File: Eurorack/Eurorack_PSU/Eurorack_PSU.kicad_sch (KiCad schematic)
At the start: 18 parts, among them J1 AC, J2 AC, U1 LM7812_TO220, U2 LM7912_TO220

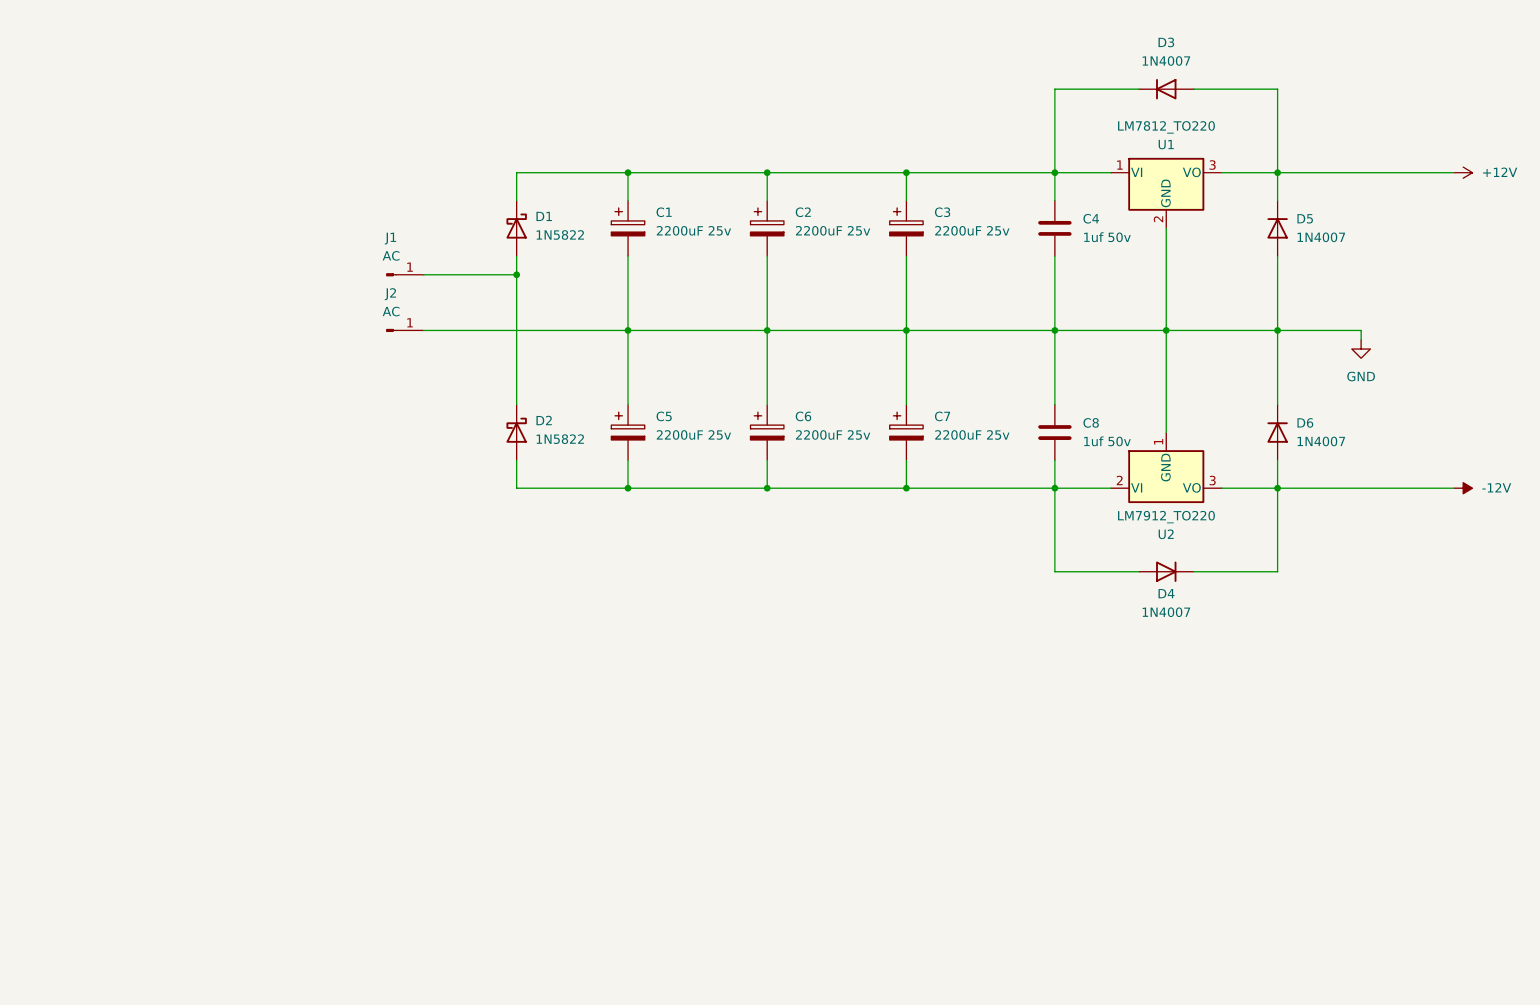
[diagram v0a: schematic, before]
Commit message: Update PSU and add more spice models
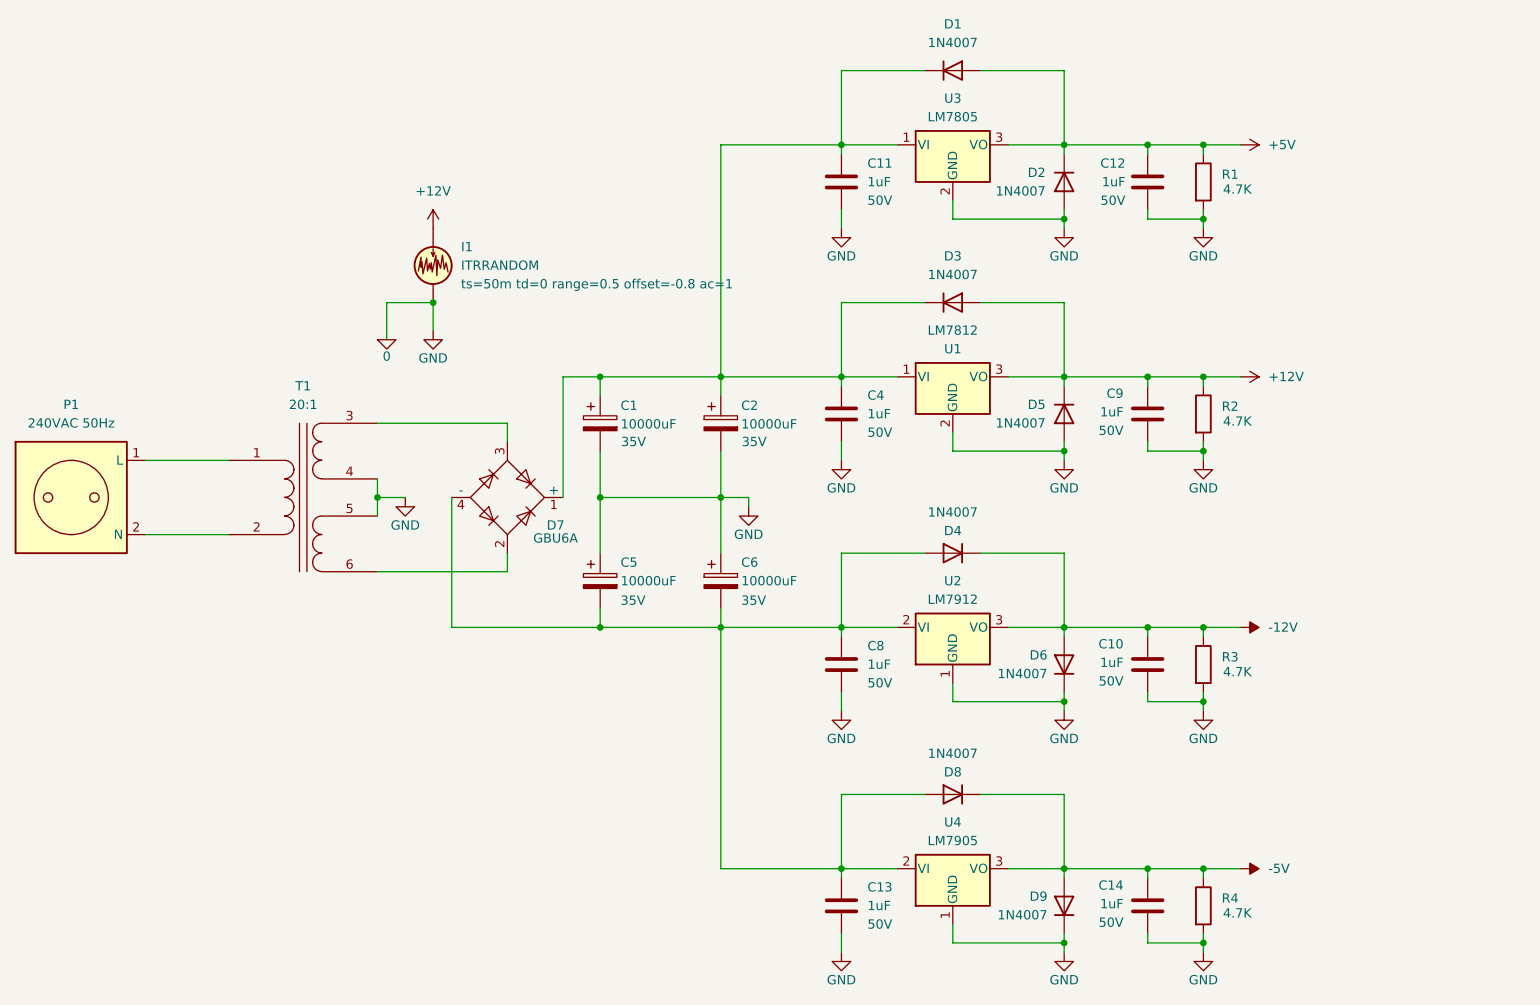
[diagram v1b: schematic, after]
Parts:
- removed C3, C7: 2200uF 25v, Capacitor_THT:CP_Radial_D16.0mm_P7.50mm, symbol Device:C_Polarized
- removed D1, D2: 1N5822, Diode_THT:D_DO-201AD_P15.24mm_Horizontal, symbol Diode:1N5822
- removed J1, J2: AC, Connector_Wire:SolderWire-1sqmm_1x01_D1.4mm_OD3.9mm, symbol Connector:Conn_01x01_Pin
- added C10, C11, C12, C13, C14, C9: 1uF, Capacitor_THT:C_Disc_D3.4mm_W2.1mm_P2.50mm, symbol Device:C
- added D1, D2, D8, D9: 1N4007, Diode_THT:D_DO-41_SOD81_P10.16mm_Horizontal, symbol Diode:1N4007
- added D7: GBU6A, Diode_THT:Diode_Bridge_Vishay_GBU, symbol Diode_Bridge:GBU6A
- added I1: ITRRANDOM, symbol Simulation_SPICE:ITRRANDOM
- added P1: 240VAC 50Hz, Connector_Wire:SolderWire-0.75sqmm_1x02_P7mm_D1.25mm_OD3.5mm, symbol Connector:Conn_Plug_2P
- added R1, R2, R3, R4: 4.7K, symbol Device:R
- added T1: 20:1, Connector_Wire:SolderWire-0.75sqmm_1x04_P7mm_D1.25mm_OD3.5mm, symbol Device:Transformer_1P_2S
- added U3: LM7805, Package_TO_SOT_THT:TO-220-3_Vertical, symbol Regulator_Linear:LM7805_TO220
- added U4: LM7905, Package_TO_SOT_THT:TO-220-3_Vertical, symbol Regulator_Linear:LM7905_TO220
- C1, C2, C5, C6: value 2200uF 25v -> 10000uF; footprint Capacitor_THT:CP_Radial_D16.0mm_P7.50mm -> Capacitor_THT:CP_Radial_D25.0mm_P10.00mm_SnapIn; Voltage (none) -> 35V
- C4, C8: value 1uf 50v -> 1uF; Voltage (none) -> 50V
- U1: value LM7812_TO220 -> LM7812
- U2: value LM7912_TO220 -> LM7912
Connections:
- net +12V: now also C9.1, I1.1, R2.1
- net -12V: now also C10.1, R3.1
- net at C5.2, C6.2, D4.2 (A)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: now also C8.1, C13.1, D7.4 (-), D8.2 (A), U4.2 (VI); no longer C8.2
- net at C1.1, C2.1, C4.1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: now also C11.1, D1.1 (K), D7.1 (+), U3.1 (VI)
- net GND renamed 0
- net 0: now also C8.2, C10.2, C11.2, C12.2, C13.2, C14.2, C9.2, D2.2 (A), D9.1 (K), I1.2, R1.2, R2.2, R3.2, R4.2, T1.4 (SB), T1.5 (SC), U3.2 (GND), U4.1 (GND); no longer C8.1
- new net: D7.2, T1.6 (SD)
- new net: D7.3, T1.3 (SA)
- new net: P1.1 (L), T1.1 (AA)
- new net: P1.2 (N), T1.2 (AB)
- new net +5V: C12.1, D1.2 (A), D2.1 (K), R1.1, U3.3 (VO)
- new net -5V: C14.1, D8.1 (K), D9.2 (A), R4.1, U4.3 (VO)
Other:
- company: (none) -> Mitch Reynolds
- title: (none) -> Eurorack_PSU
- moved on the sheet: C1, C4, D3, D4, D5, D6, U1, U2
